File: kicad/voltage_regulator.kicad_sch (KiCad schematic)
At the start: 4 parts, among them U4 MIC5219-3.3YM5-TR

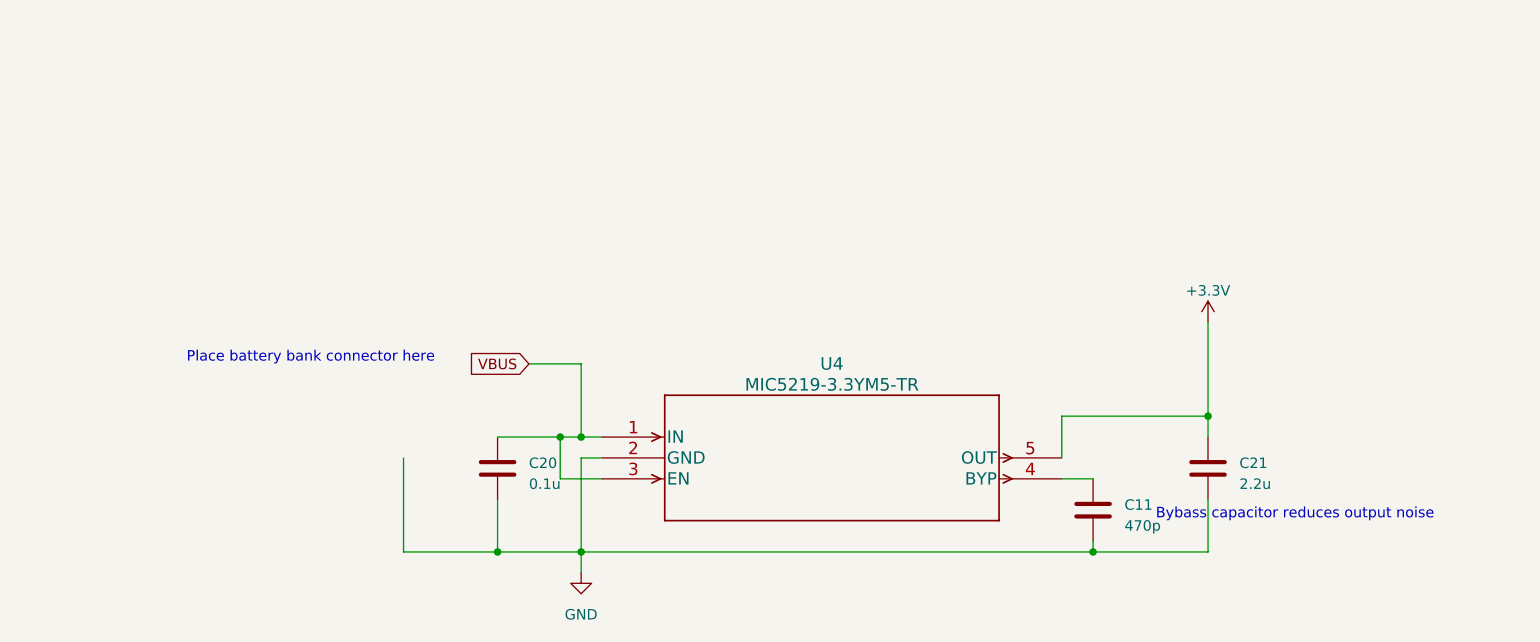
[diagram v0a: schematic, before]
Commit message: voltage regulator update
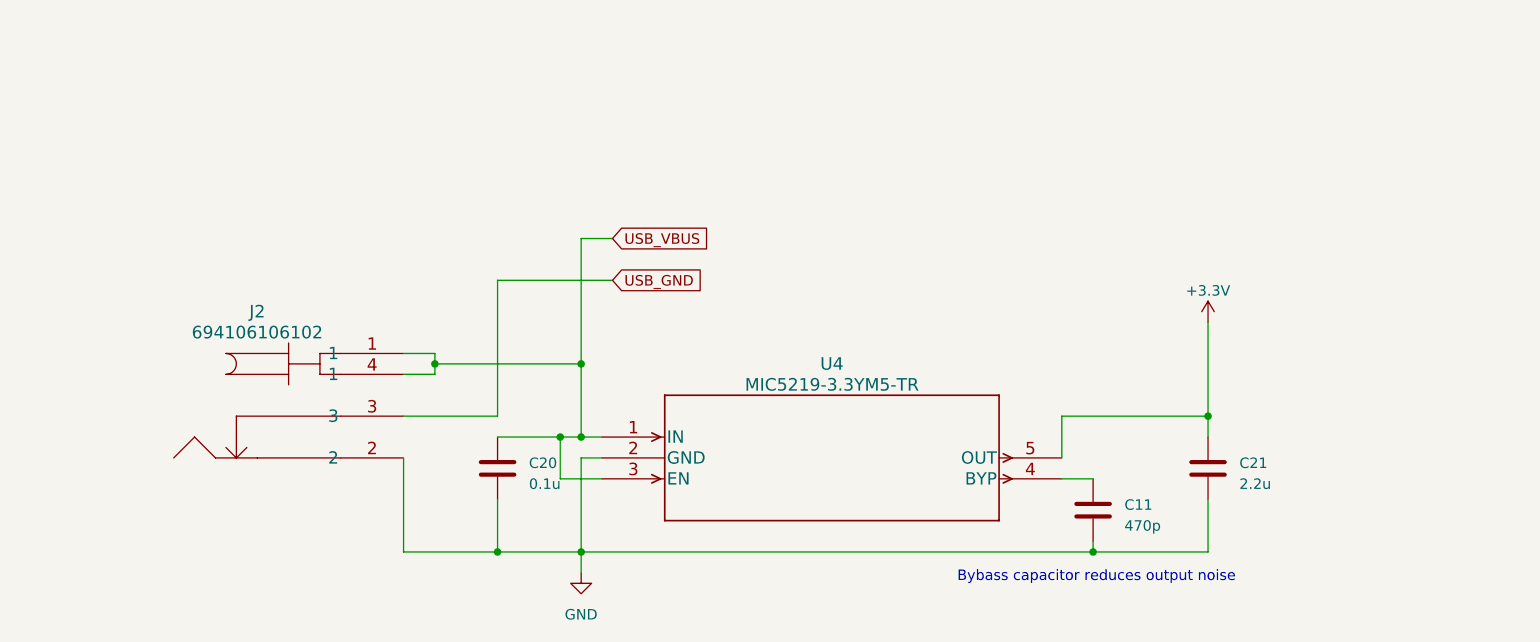
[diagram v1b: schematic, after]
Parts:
- added J2: 694106106102, CONN4_8106102_WRE, symbol 694106106102:694106106102
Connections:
- net GND: now also J2.2
- net VBUS renamed USB_VBUS
- net USB_VBUS: now also J2.1, J2.4 (1)
- new net USB_GND: J2.3
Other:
- note removed: "Place battery bank connector here"
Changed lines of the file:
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@@
   (junction (at 96.52 78.74) (diameter 0) (color 0 0 0 0)
   )
+  (junction (at 81.28 69.85) (diameter 0) (color 0 0 0 0)
+  )
+  (junction (at 99.06 69.85) (diameter 0) (color 0 0 0 0)
+  )
+  (junction (at 88.9 92.71) (diameter 0) (color 0 0 0 0)
+  )
   (junction (at 175.26 76.2) (diameter 0) (color 0 0 0 0)
   )
-  (junction (at 88.9 92.71) (diameter 0) (color 0 0 0 0)
-  )
   (junction (at 99.06 92.71) (diameter 0) (color 0 0 0 0)
   )
@@
     (stroke (width 0) (type default))
   )
+  (wire (pts (xy 77.47 68.58) (xy 81.28 68.58))
+    (stroke (width 0) (type default))
+  )
+  (wire (pts (xy 102.87 54.61) (xy 99.06 54.61))
+    (stroke (width 0) (type default))
+  )
   (wire (pts (xy 175.26 76.2) (xy 175.26 78.74))
     (stroke (width 0) (type default))
@@
     (stroke (width 0) (type default))
   )
+  (wire (pts (xy 77.47 71.12) (xy 81.28 71.12))
+    (stroke (width 0) (type default))
+  )
+  (wire (pts (xy 77.47 76.2) (xy 88.9 76.2))
+    (stroke (width 0) (type default))
+  )
   (wire (pts (xy 88.9 78.74) (xy 96.52 78.74))
     (stroke (width 0) (type default))
@@
     (stroke (width 0) (type default))
   )
-  (wire (pts (xy 92.71 69.85) (xy 99.06 69.85))
+  (wire (pts (xy 99.06 54.61) (xy 99.06 69.85))
+    (stroke (width 0) (type default))
+  )
+  (wire (pts (xy 81.28 69.85) (xy 99.06 69.85))
     (stroke (width 0) (type default))
   )
@@
     (stroke (width 0) (type default))
   )
+  (wire (pts (xy 81.28 71.12) (xy 81.28 69.85))
+    (stroke (width 0) (type default))
+  )
   (wire (pts (xy 99.06 92.71) (xy 99.06 95.25))
     (stroke (width 0) (type default))
@@
     (stroke (width 0) (type default))
   )
+  (wire (pts (xy 77.47 92.71) (xy 88.9 92.71))
+    (stroke (width 0) (type default))
+  )
+  (wire (pts (xy 77.47 81.28) (xy 77.47 92.71))
+    (stroke (width 0) (type default))
+  )
+  (wire (pts (xy 88.9 59.69) (xy 102.87 59.69))
+    (stroke (width 0) (type default))
+  )
+  (wire (pts (xy 81.28 68.58) (xy 81.28 69.85))
+    (stroke (width 0) (type default))
+  )
   (wire (pts (xy 161.29 92.71) (xy 175.26 92.71))
     (stroke (width 0) (type default))
   )
-  (wire (pts (xy 77.47 92.71) (xy 88.9 92.71))
-    (stroke (width 0) (type default))
-  )
-  (wire (pts (xy 77.47 81.28) (xy 77.47 92.71))
-    (stroke (width 0) (type default))
-  )
   (wire (pts (xy 88.9 86.36) (xy 88.9 92.71))
     (stroke (width 0) (type default))
@@
     (stroke (width 0) (type default))
   )
+  (wire (pts (xy 88.9 76.2) (xy 88.9 59.69))
+    (stroke (width 0) (type default))
+  )
   (wire (pts (xy 96.52 78.74) (xy 99.06 78.74))
     (stroke (width 0) (type default))
   )
-  (text "Bybass capacitor reduces output noise" (at 168.91 88.9 0)
+  (text "Bybass capacitor reduces output noise" (at 144.78 96.52 0)
     (effects (font (size 1.27 1.27)) (justify left bottom))
   )
-  (text "Place battery bank connector here" (at 81.28 69.85 0)
-    (effects (font (size 1.27 1.27)) (justify right bottom))
-  )
-  (global_label "VBUS" (shape input) (at 92.71 69.85 180) (fields_autoplaced)
-    (effects (font (size 1.27 1.27)) (justify right))
-    (property "Intersheetrefs" "${INTERSHEET_REFS}" (at 84.9056 69.85 0)
-      (effects (font (size 1.27 1.27)) (justify right) hide)
+  (global_label "USB_GND" (shape input) (at 102.87 59.69 0) (fields_autoplaced)
+    (effects (font (size 1.27 1.27)) (justify left))
+    (property "Intersheetrefs" "${INTERSHEET_REFS}" (at 114.4239 59.69 0)
+      (effects (font (size 1.27 1.27)) (justify left) hide)
+    )
+  )
+  (global_label "USB_VBUS" (shape input) (at 102.87 54.61 0) (fields_autoplaced)
+    (effects (font (size 1.27 1.27)) (justify left))
+    (property "Intersheetrefs" "${INTERSHEET_REFS}" (at 115.452 54.61 0)
+      (effects (font (size 1.27 1.27)) (justify left) hide)
     )
   )
@@
         )
       )
+    )
+  )
+  (symbol (lib_id "694106106102:694106106102") (at 77.47 68.58 0) (mirror y) (unit 1)
+    (in_bom yes) (on_board yes) (dnp no) (fields_autoplaced)
+    (property "Reference" "J2" (at 59.69 63.5 0)
+      (effects (font (size 1.524 1.524)))
+    )
+    (property "Value" "694106106102" (at 59.69 66.04 0)
+      (effects (font (size 1.524 1.524)))
+    )
+    (property "Footprint" "CONN4_8106102_WRE" (at 67.31 65.024 0)
+      (effects (font (size 1.524 1.524)) hide)
+    )
+    (property "Datasheet" "" (at 77.47 68.58 0)
+      (effects (font (size 1.524 1.524)))
+    )
+    (pin "1")
+    (pin "2")
+    (pin "3")
+    (pin "4")
+    (instances
+      (project "IoT_sulari"
+        (path "/184b47ed-2c2b-4c02-be35-d18f4f4e5685/900a775e-83e7-4530-ab2f-7e5f26c05ece"
+          (reference "J2") (unit 1)
+        )
+      )

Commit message: added comments and muokkasin komponenttiennumeroinnin selvemmäksi.
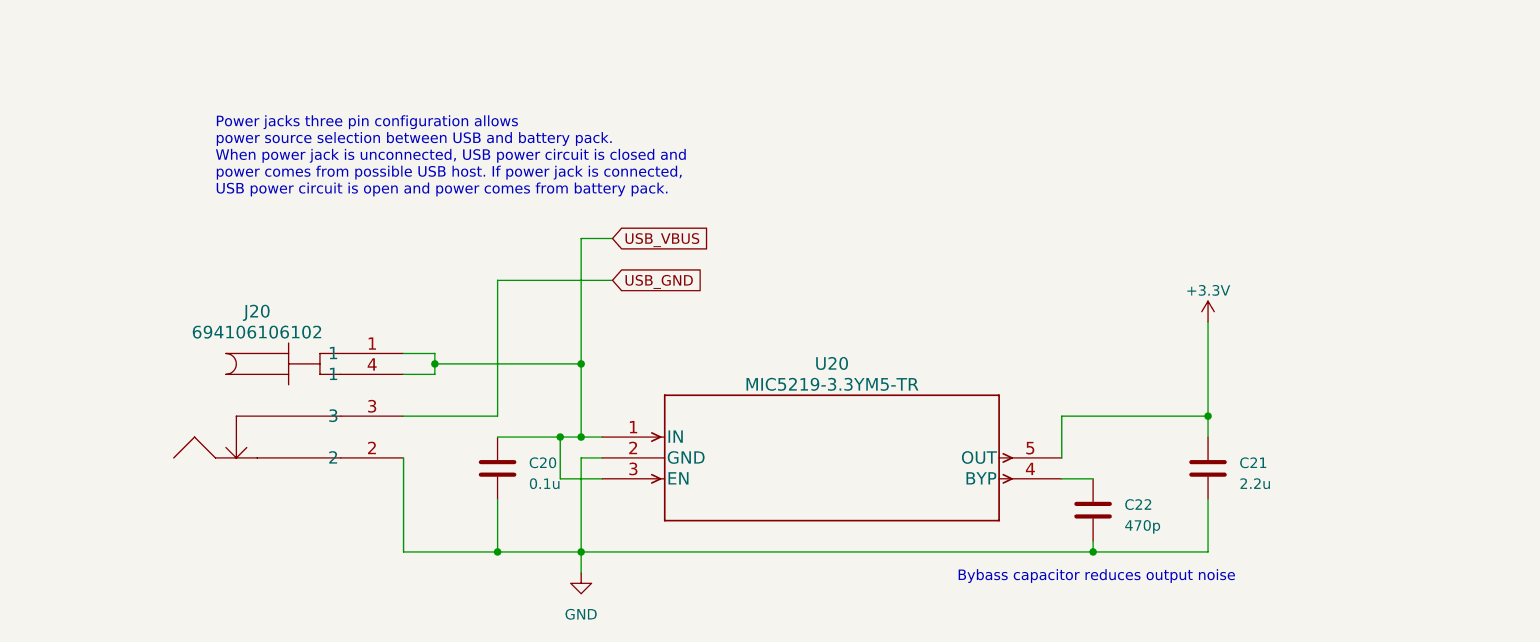
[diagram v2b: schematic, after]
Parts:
- renumbered C11 to C22, J2 to J20, U4 to U20
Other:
- note added: "Power jacks three pin configuration allows power source selection between USB and battery pack. When power jack is unconnected, USB power circuit is closed and power comes from possible USB host. If power jack is connected, USB power circuit is open and power comes from battery pack."
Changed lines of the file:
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@@
+    (effects (font (size 1.27 1.27)) (justify left bottom))
+  )
+  (text "Power jacks three pin configuration allows \npower source selection between USB and battery pack.\nWhen power jack is unconnected, USB power circuit is closed and \npower comes from possible USB host. If power jack is connected,\nUSB power circuit is open and power comes from battery pack."
+    (at 54.61 49.53 0)
     (effects (font (size 1.27 1.27)) (justify left bottom))
   )
@@
   (symbol (lib_id "Device:C") (at 161.29 87.63 0) (unit 1)
     (in_bom yes) (on_board yes) (dnp no) (fields_autoplaced)
-    (property "Reference" "C11" (at 165.1 86.995 0)
+    (property "Reference" "C22" (at 165.1 86.995 0)
       (effects (font (size 1.27 1.27)) (justify left))
     )
@@
       (project "IoT_sulari"
         (path "/184b47ed-2c2b-4c02-be35-d18f4f4e5685/900a775e-83e7-4530-ab2f-7e5f26c05ece"
-          (reference "C11") (unit 1)
+          (reference "C22") (unit 1)
         )
       )
@@
   (symbol (lib_id "MIC5219-3.3YM5-TR:MIC5219-3.3YM5-TR") (at 101.6 78.74 0) (unit 1)
     (in_bom yes) (on_board yes) (dnp no) (fields_autoplaced)
-    (property "Reference" "U4" (at 129.54 69.85 0)
+    (property "Reference" "U20" (at 129.54 69.85 0)
       (effects (font (size 1.524 1.524)))
     )
@@
       (project "IoT_sulari"
         (path "/184b47ed-2c2b-4c02-be35-d18f4f4e5685/900a775e-83e7-4530-ab2f-7e5f26c05ece"
-          (reference "U4") (unit 1)
+          (reference "U20") (unit 1)
         )
       )
@@
   (symbol (lib_id "694106106102:694106106102") (at 77.47 68.58 0) (mirror y) (unit 1)
     (in_bom yes) (on_board yes) (dnp no) (fields_autoplaced)
-    (property "Reference" "J2" (at 59.69 63.5 0)
+    (property "Reference" "J20" (at 59.69 63.5 0)
       (effects (font (size 1.524 1.524)))
     )
@@
       (project "IoT_sulari"
         (path "/184b47ed-2c2b-4c02-be35-d18f4f4e5685/900a775e-83e7-4530-ab2f-7e5f26c05ece"
-          (reference "J2") (unit 1)
+          (reference "J20") (unit 1)
         )
       )

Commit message: Added Digikey part number and footprint to symbols, added signal TMP_ALERT
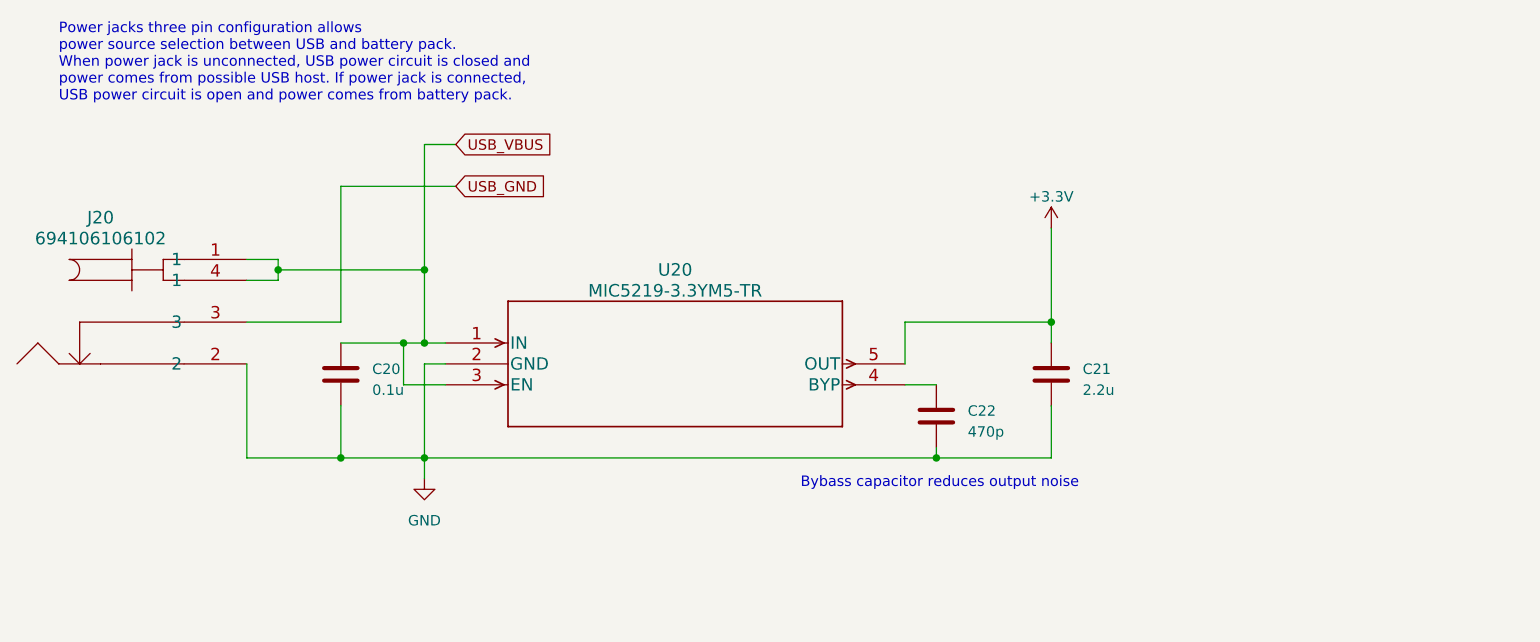
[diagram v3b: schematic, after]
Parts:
- J20: footprint CONN4_8106102_WRE -> 694106106102:694106106102; Digikey (none) -> 732-5929-1-ND
- U20: footprint SOT-23-5_M5_MCH -> MIC5219-3.3YM5-TR:MIC5219-3.3YM5-TR; Digikey (none) -> 576-1281-1-ND
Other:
- moved on the sheet: C20, C21, C22, J20, U20

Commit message: Added buttons and connectors
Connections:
- net USB_GND is gone; now on net GND: J20.3
- net USB_VBUS: no longer names the net of C20.1, J20.1, J20.4 (1), U20.1 (IN), U20.3 (EN)
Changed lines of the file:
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@@
   (junction (at 62.23 58.42) (diameter 0) (color 0 0 0 0)
   )
-  (junction (at 80.01 58.42) (diameter 0) (color 0 0 0 0)
+  (junction (at 58.42 69.85) (diameter 0) (color 0 0 0 0)
   )
   (junction (at 69.85 81.28) (diameter 0) (color 0 0 0 0)
@@
     (stroke (width 0) (type default))
   )
-  (wire (pts (xy 83.82 43.18) (xy 80.01 43.18))
+  (wire (pts (xy 58.42 64.77) (xy 58.42 69.85))
     (stroke (width 0) (type default))
   )
@@
     (stroke (width 0) (type default))
   )
-  (wire (pts (xy 58.42 64.77) (xy 69.85 64.77))
-    (stroke (width 0) (type default))
-  )
   (wire (pts (xy 69.85 67.31) (xy 77.47 67.31))
     (stroke (width 0) (type default))
   )
   (wire (pts (xy 80.01 67.31) (xy 82.55 67.31))
-    (stroke (width 0) (type default))
-  )
-  (wire (pts (xy 80.01 43.18) (xy 80.01 58.42))
     (stroke (width 0) (type default))
   )
@@
     (stroke (width 0) (type default))
   )
-  (wire (pts (xy 69.85 48.26) (xy 83.82 48.26))
-    (stroke (width 0) (type default))
-  )
   (wire (pts (xy 62.23 57.15) (xy 62.23 58.42))
     (stroke (width 0) (type default))
@@
     (stroke (width 0) (type default))
   )
-  (wire (pts (xy 69.85 64.77) (xy 69.85 48.26))
-    (stroke (width 0) (type default))
-  )
   (wire (pts (xy 77.47 67.31) (xy 80.01 67.31))
     (stroke (width 0) (type default))
@@
     (effects (font (size 1.27 1.27)) (justify left bottom))
   )
-  (global_label "USB_GND" (shape input) (at 83.82 48.26 0) (fields_autoplaced)
-    (effects (font (size 1.27 1.27)) (justify left))
-    (property "Intersheetrefs" "${INTERSHEET_REFS}" (at 95.3739 48.26 0)
-      (effects (font (size 1.27 1.27)) (justify left) hide)
-    )
-  )
-  (global_label "USB_VBUS" (shape input) (at 83.82 43.18 0) (fields_autoplaced)
-    (effects (font (size 1.27 1.27)) (justify left))
-    (property "Intersheetrefs" "${INTERSHEET_REFS}" (at 96.402 43.18 0)
-      (effects (font (size 1.27 1.27)) (justify left) hide)
-    )
-  )
   (symbol (lib_id "Device:C") (at 142.24 76.2 0) (unit 1)

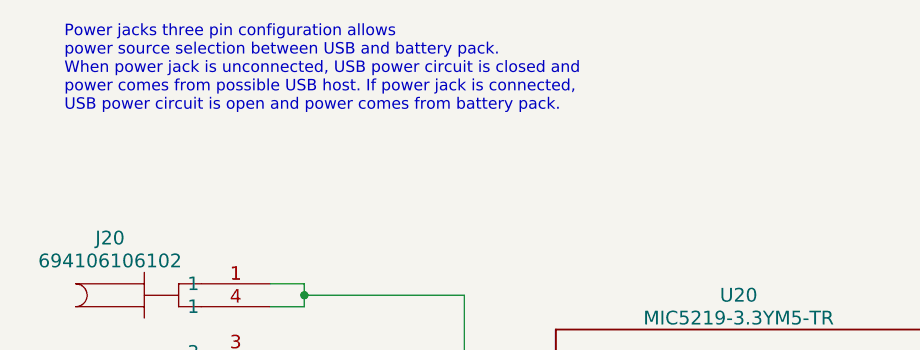
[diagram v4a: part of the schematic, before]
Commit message: USB-module delete
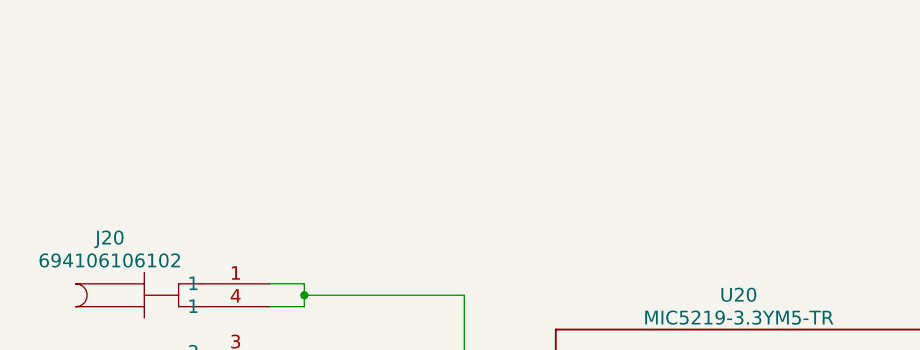
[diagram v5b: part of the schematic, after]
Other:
- note removed: "Power jacks three pin configuration allows power source selection between USB and battery pack. When power jack is unconnected, USB power circuit is closed and power comes from possible USB host. If power jack is connected, USB power circuit is open and power comes from battery pack."
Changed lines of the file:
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@@
-    (effects (font (size 1.27 1.27)) (justify left bottom))
-  )
-  (text "Power jacks three pin configuration allows \npower source selection between USB and battery pack.\nWhen power jack is unconnected, USB power circuit is closed and \npower comes from possible USB host. If power jack is connected,\nUSB power circuit is open and power comes from battery pack."
-    (at 35.56 38.1 0)
     (effects (font (size 1.27 1.27)) (justify left bottom))
   )
